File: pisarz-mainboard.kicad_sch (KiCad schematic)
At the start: 0 parts

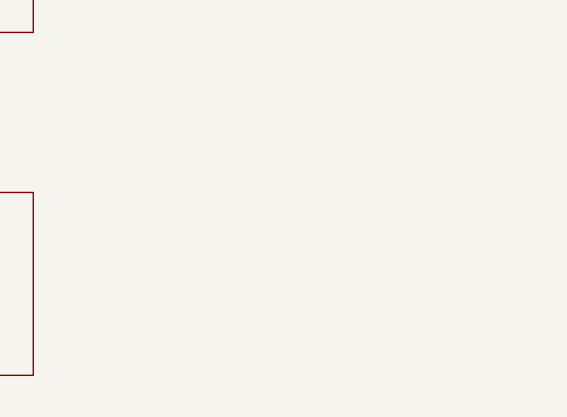
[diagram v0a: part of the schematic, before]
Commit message: Add PWM controllers to schematic
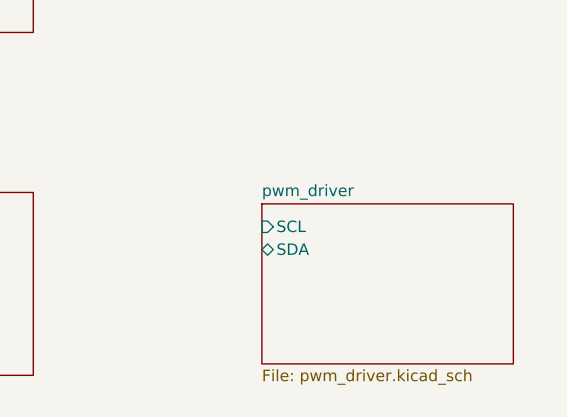
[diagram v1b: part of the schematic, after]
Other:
- added sheet pwm_driver (pwm_driver.kicad_sch)
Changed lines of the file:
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@@
 	(paper "A4")
+	(sheet
+		(at 182.88 81.28)
+		(size 27.94 17.78)
+		(exclude_from_sim no)
+		(in_bom yes)
+		(on_board yes)
+		(dnp no)
+		(fields_autoplaced yes)
+		(stroke
+			(width 0.1524)
+			(type solid)
+		)
+		(fill
+			(color 0 0 0 0)
+		)
+		(property "Sheetname" "pwm_driver"
+			(at 182.88 80.5684 0)
+			(show_name no)
+			(do_not_autoplace no)
+			(effects
+				(font
+					(size 1.27 1.27)
+				)
+				(justify left bottom)
+			)
+		)
+		(property "Sheetfile" "pwm_driver.kicad_sch"
+			(at 182.88 99.6446 0)
+			(show_name no)
+			(do_not_autoplace no)
+			(effects
+				(font
+					(size 1.27 1.27)
+				)
+				(justify left top)
+			)
+		)
+		(pin "SCL" input
+			(at 182.88 83.82 180)
+			(effects
+				(font
+					(size 1.27 1.27)
+				)
+				(justify left)
+			)
+		)
+		(pin "SDA" bidirectional
+			(at 182.88 86.36 180)
+			(effects
+				(font
+					(size 1.27 1.27)
+				)
+				(justify left)
+			)
+		)
+		(instances
+			(project "pisarz-mainboard"
+				(path "/3fa3a621-8f50-4a33-bd41-24b098d8d0ef"
+					(page "5")
+				)
+			)
+		)
+	)
 	(sheet
 		(at 127 80.01)

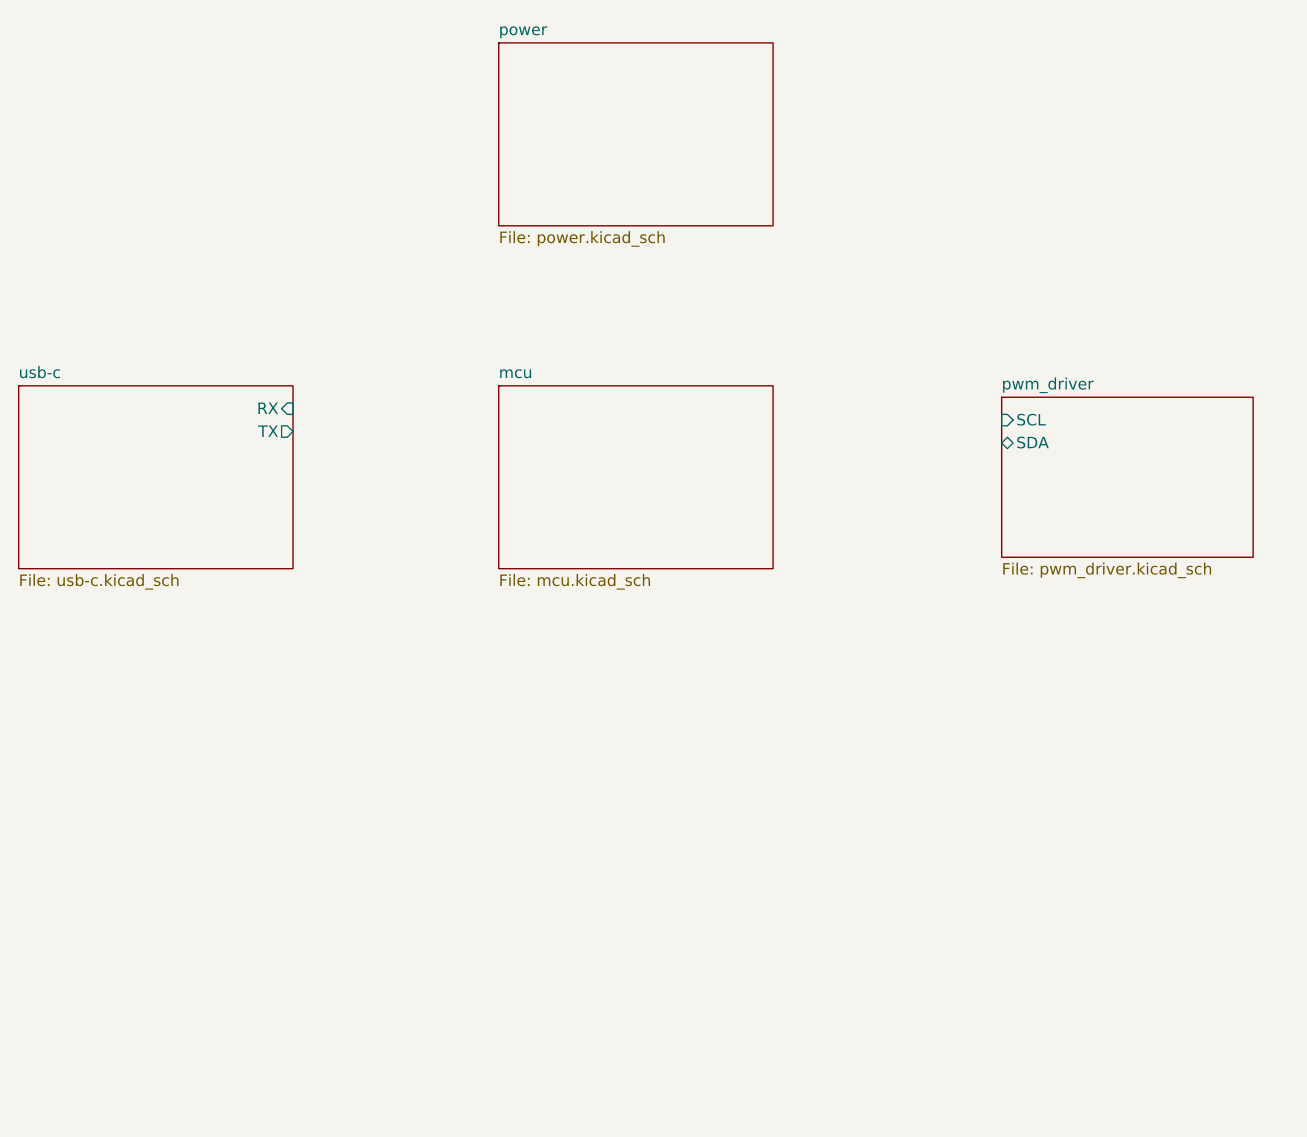
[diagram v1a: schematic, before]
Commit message: Add servo connectors
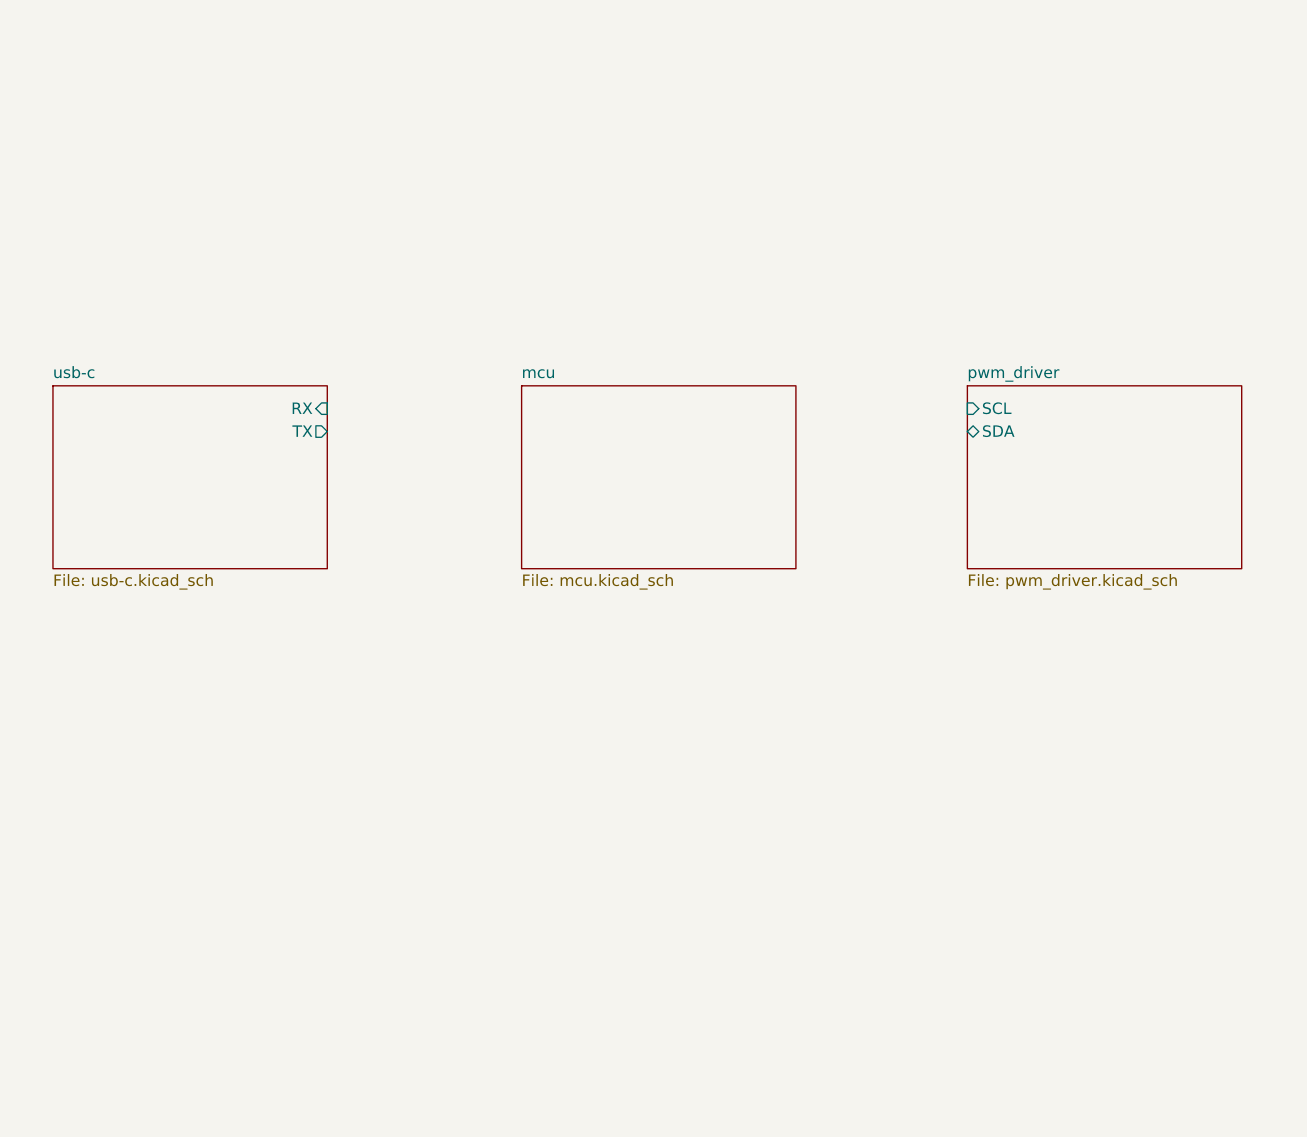
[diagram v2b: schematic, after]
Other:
- removed sheet power
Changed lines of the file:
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@@
 	(paper "A4")
 	(sheet
-		(at 182.88 81.28)
-		(size 27.94 17.78)
+		(at 179.07 80.01)
+		(size 30.48 20.32)
 		(exclude_from_sim no)
 		(in_bom yes)
@@
 		)
 		(property "Sheetname" "pwm_driver"
-			(at 182.88 80.5684 0)
+			(at 179.07 79.2984 0)
 			(show_name no)
 			(do_not_autoplace no)
@@
 		)
 		(property "Sheetfile" "pwm_driver.kicad_sch"
-			(at 182.88 99.6446 0)
+			(at 179.07 100.9146 0)
 			(show_name no)
 			(do_not_autoplace no)
@@
 		)
 		(pin "SCL" input
-			(at 182.88 83.82 180)
+			(at 179.07 82.55 180)
 			(effects
 				(font
@@
 		)
 		(pin "SDA" bidirectional
-			(at 182.88 86.36 180)
+			(at 179.07 85.09 180)
 			(effects
 				(font
@@
 	)
 	(sheet
-		(at 127 80.01)
+		(at 129.54 80.01)
 		(size 30.48 20.32)
 		(exclude_from_sim no)
@@
 		)
 		(property "Sheetname" "mcu"
-			(at 127 79.2984 0)
+			(at 129.54 79.2984 0)
 			(show_name no)
 			(do_not_autoplace no)
@@
 		)
 		(property "Sheetfile" "mcu.kicad_sch"
-			(at 127 100.9146 0)
+			(at 129.54 100.9146 0)
 			(show_name no)
 			(do_not_autoplace no)
@@
 	)
 	(sheet
-		(at 73.66 80.01)
+		(at 77.47 80.01)
 		(size 30.48 20.32)
 		(exclude_from_sim no)
@@
 		)
 		(property "Sheetname" "usb-c"
-			(at 73.66 79.2984 0)
+			(at 77.47 79.2984 0)
 			(show_name no)
 			(do_not_autoplace no)
@@
 		)
 		(property "Sheetfile" "usb-c.kicad_sch"
-			(at 73.66 100.9146 0)
+			(at 77.47 100.9146 0)
 			(show_name no)
 			(do_not_autoplace no)
@@
 		)
 		(pin "RX" input
-			(at 104.14 82.55 0)
+			(at 107.95 82.55 0)
 			(effects
 				(font
@@
 		)
 		(pin "TX" output
-			(at 104.14 85.09 0)
+			(at 107.95 85.09 0)
 			(effects
 				(font
@@
 				)
 			)
-		)
-	)
-	(sheet
-		(at 127 41.91)
-		(size 30.48 20.32)
-		(exclude_from_sim no)
-		(in_bom yes)
-		(on_board yes)
-		(dnp no)
-		(fields_autoplaced yes)
-		(stroke
-			(width 0.1524)
-			(type solid)
-		)
-		(fill
-			(color 0 0 0 0)
-		)
-		(property "Sheetname" "power"
-			(at 127 41.1984 0)
-			(show_name no)
-			(do_not_autoplace no)
-			(effects
-				(font
-					(size 1.27 1.27)
-				)
-				(justify left bottom)
-			)
-		)
-		(property "Sheetfile" "power.kicad_sch"
-			(at 127 62.8146 0)
-			(show_name no)
-			(do_not_autoplace no)
-			(effects
-				(font
-					(size 1.27 1.27)
-				)
-				(justify left top)
-			)
-		)
-		(instances
-			(project "pisarz-mainboard"
-				(path "/3fa3a621-8f50-4a33-bd41-24b098d8d0ef"
-					(page "4")
-				)
-			)

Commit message: Update schematic
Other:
- sheet pwm_driver renamed pwm-driver
- added sheet esp32-module-connector (esp32_module_connector.kicad_sch)
- added sheet usb-c-dfu (usb_c_dfu.kicad_sch)
- sheet mcu ports: added I2C_SCL, I2C_SDA, UART1_RX, UART1_TX, UART2_RX, UART2_TX, USB_D+, USB_D-; removed none
- sheet usb-c: file usb-c.kicad_sch -> usb_c.kicad_sch
- sheet usb-c ports: added CP2102_RX, CP2102_TX; removed RX, TX
